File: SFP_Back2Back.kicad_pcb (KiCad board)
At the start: 2 copper layers, 80 x 50 mm, 42 parts, among them J1 Conn_01x04, J101 Barrel_Jack, J2 Conn_01x03, J201 SFP, J3 Conn_01x03, J301 SFP, U1 LM2576S-3.3

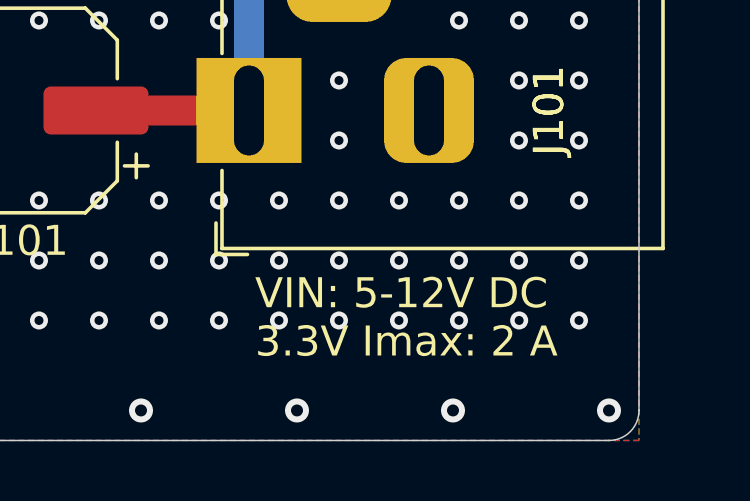
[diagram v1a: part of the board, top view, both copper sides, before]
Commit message: Fixed LCSC Order Number for 68R Resistor
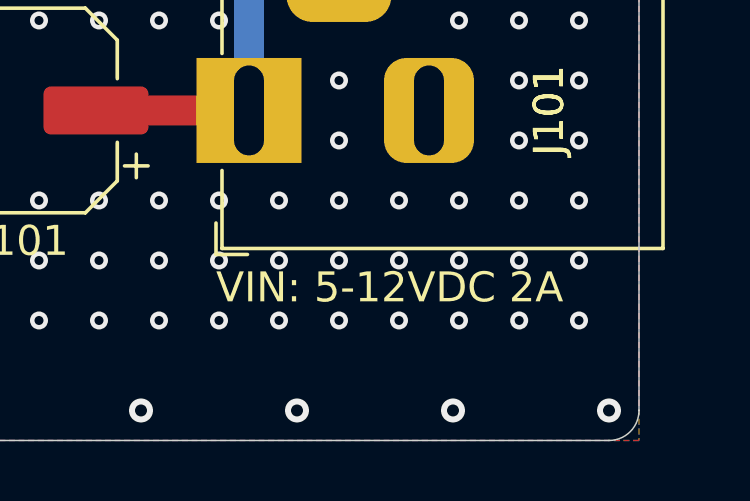
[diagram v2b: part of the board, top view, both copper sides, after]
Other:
- board text added: "VIN: 5-12VDC 2A"
- board text removed: "VIN: 5-12V DC 3.3V Imax: 2 A"
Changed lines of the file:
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@@
     (descr "Resistor SMD 0805 (2012 Metric), square (rectangular) end terminal, IPC_7351 nominal, (Body size source: IPC-SM-782 page 72, https://www.pcb-3d.com/wordpress/wp-content/uploads/ipc-sm-782a_amendment_1_and_2.pdf), generated with kicad-footprint-generator")
     (tags "resistor")
-    (property "LCSC Part Number" "C474219")
+    (property "LCSC Part Number" "C17802")
     (property "Sheetfile" "SFP_Back2Back.kicad_sch")
     (property "Sheetname" "")
@@
     (effects (font (size 0.7 0.7) (thickness 0.15)))
   )
-  (gr_text "VIN: 5-12V DC\n3.3V Imax: 2 A" (at 247.2 145.9) (layer "F.SilkS")
+  (gr_text "VIN: 5-12VDC 2A" (at 245.9 144.9) (layer "F.SilkS")
     (effects (font (size 1 1) (thickness 0.15)) (justify left))
   )

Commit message: Updated README
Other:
- board text added: "github.com/Westwoodlabs/SFP-Back2Back"
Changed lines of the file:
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@@
   (gr_arc (start 259 100) (mid 259.707107 100.292893) (end 260 101) (layer "Edge.Cuts") (width 0.05))
   (gr_arc (start 260 149) (mid 259.707107 149.707107) (end 259 150) (layer "Edge.Cuts") (width 0.05))
+  (gr_text "github.com/Westwoodlabs/SFP-Back2Back" (at 214.25 145) (layer "B.SilkS")
+    (effects (font (size 1 1) (thickness 0.15)) (justify left mirror))
+  )
   (gr_text "VIN" (at 246.9 130.6 90) (layer "F.SilkS")
     (effects (font (size 1 1) (thickness 0.15)) (justify right))
